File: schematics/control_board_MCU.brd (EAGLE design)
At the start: 92.7 x 38.1 mm, 49 parts, among them J1 POWER_JACKPTH, U1 ATMEGA168, Y1 16MHZ

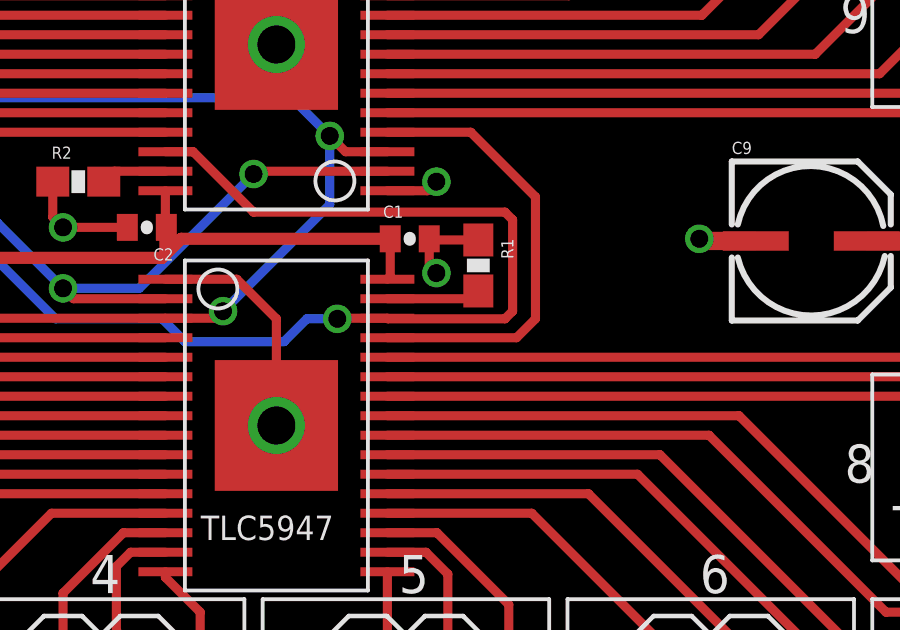
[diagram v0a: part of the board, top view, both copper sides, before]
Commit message: changed WS2812 controller to uUSB, minor spacing edits to everything else
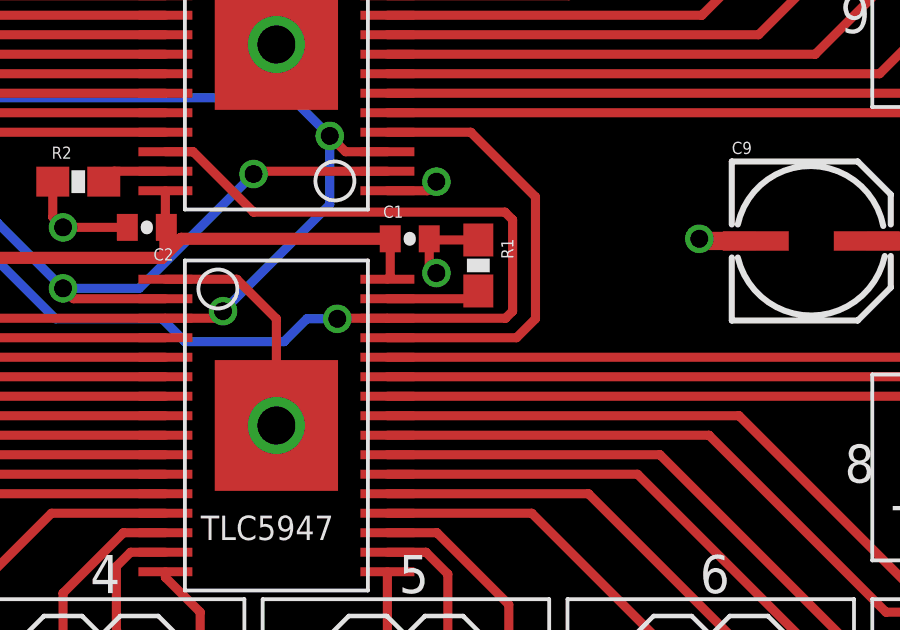
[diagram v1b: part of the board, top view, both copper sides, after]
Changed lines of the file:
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@@
 <wire x1="70.104" y1="19.812" x2="70.358" y2="19.558" width="0.3048" layer="1"/>
 <wire x1="70.358" y1="19.558" x2="70.358" y2="16.51" width="0.3048" layer="1"/>
-<wire x1="70.358" y1="16.51" x2="70.104" y2="16.256" width="0.3048" layer="1"/>
-<wire x1="70.104" y1="16.256" x2="66.203" y2="16.256" width="0.3048" layer="1"/>
-<wire x1="66.203" y1="16.256" x2="66.184" y2="16.275" width="0.3048" layer="1"/>
 <wire x1="64.516" y1="16.256" x2="63.5" y2="16.256" width="0.3048" layer="16"/>
 <wire x1="63.5" y1="16.256" x2="62.738" y2="15.494" width="0.3048" layer="16"/>
@@
 <wire x1="20.447" y1="35.941" x2="20.447" y2="26.70081875" width="0.3048" layer="16"/>
 <wire x1="20.447" y1="26.70081875" x2="20.4619375" y2="26.68588125" width="0.3048" layer="16"/>
+<wire x1="66.184" y1="16.275" x2="70.123" y2="16.275" width="0.3048" layer="1"/>
+<wire x1="70.123" y1="16.275" x2="70.358" y2="16.51" width="0.3048" layer="1"/>
 </signal>
 <signal name="BLANK">
